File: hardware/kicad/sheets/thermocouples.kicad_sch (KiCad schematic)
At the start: 18 parts, among them J3 TC1_K, J8 TC2_K, U3 MAX31856MUD+, U5 MAX31856MUD+

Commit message: hardware: hierarchical schematic, ERC at 0/0, rev B.3
Applies items 1-3 of SCHEMATIC-REVIEW-2026-10-22.md.

ERC: the 173 lib_symbol_mismatch warnings were over-escaped quotes in the
embedded power symbols' Description strings; refreshed from the library.
The 18 off-grid power symbols are snapped and their stub wires redrawn.
The VIN and VLED global labels that existed only to carry a PWR_FLAG are
gone; the flags now sit on the nets they drive (J2.1, the VLED junction).
ERC reads 0 errors / 0 warnings with the documented SDO exclusion.

Hierarchy: no global labels remain. Each net that crosses sheets has one
hierarchical label per sheet, matching sheet pins on the root, and the
root wires those pins as a block diagram. Every other former global label
is a local label. The eight signal test points (TP4-TP11) move from the
test sheet to the mcu and ct sheets beside their nets, so the test block
needs no pins. KiCad names the nets /mcu/SPI_MISO etc.; netlist.py strips
the path, so the board's net names and the routing tables are unchanged
(182 components, 538 pads, 0 mismatches). single_global_label is now a
warning. check_sync_idempotent's collision fixture used the bare
"SPI_MISO" name and is updated, with a loud failure if its victims vanish.

Drawing: rev B.3 dated 2026-10-22 on every sheet, ct on A3 like the rest,
the three overflowing titles shortened, and the notes no longer refer to
design.py or to crystal load caps that no longer exist.

Co-Authored-By: Claude Fable 5.1 <noreply@anthropic.com>
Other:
- title: Bisque Kiln Controller - Thermocouple front-ends (MAX31856 x2) -> Bisque Kiln Controller - Thermocouple front-ends

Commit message: hardware: flags at their sources, tri-state MAX31856, Q4 flipped, make erc
Second batch from SCHEMATIC-REVIEW-2026-10-22.md (findings 5, 7, 14, 15,
16 and the local half of 19).

PWR_FLAGs: the power sheet's parked corner is gone. Each flag now sits
where its rail is created - J2.1 (VIN), J2.2 (GND), Q8 source (VIN_P),
L1 output (BUCK_5V) and J1 pin A4 (VBUS, on the mcu sheet) - with the
value text shown on all of them.

MAX31856: U3 and U5 now use bisque:MAX31856 from the new project library
bisque.kicad_sym (registered in sym-lib-table), a copy of the KiCad
symbol with SDO typed tri-state, which is what the part does while CS is
high. The ERC exclusion that papered over the shared SPI_MISO is removed;
ERC is clean with no exclusions.

Q4 is mirrored so the high-side P-FET reads source-up to +5V and drain
down to SSR_EN. One Value string per LCSC part (C38/C44/C45 22uF/25V,
R11 100R 1%); C46 moved 5 mm right to clear the longer text. Every test
point's Value is its net name (TP1 "+3V3" ... TP12 "WDT_CT_P"), so the
board's Value fields, the JLC BOM and the schematic PDF regenerate.

make erc runs kicad-cli ERC at every severity and fails on any
violation; lib_symbol_mismatch, endpoint_off_grid and
same_local_global_label are promoted to errors in the project. It is not
part of pcb-check or CI on purpose.

Board: sync changed only Value fields (0 re-netted); gerbers differ by
timestamp only; DRC 0; full make pcb-check passes.

Co-Authored-By: Claude Fable 5.1 <noreply@anthropic.com>
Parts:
- U3, U5: symbol Sensor_Temperature:MAX31856 -> bisque:MAX31856
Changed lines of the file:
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@@
 	)
 	(symbol
-		(lib_id "Sensor_Temperature:MAX31856")
+		(lib_id "bisque:MAX31856")
 		(at 186.69 80.01 0)
 		(unit 1)
@@
 	)
 	(symbol
-		(lib_id "Sensor_Temperature:MAX31856")
+		(lib_id "bisque:MAX31856")
 		(at 60.96 80.01 0)
 		(unit 1)

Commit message: hardware: honest symbols, real MPNs, U6 spares grounded, LCD_RST verified
Third batch from SCHEMATIC-REVIEW-2026-10-22.md (findings 6, 8, 11, 17,
18 and E1/E2).

Symbols: D8 is bisque:SMAJ30A (drawn as a zener with its cathode on the
rail, since the fitted TVS is unidirectional), Q5-Q7 are bisque:CJ2310
and U2 is bisque:TLV1117LV33, each a flattened copy of the stock symbol
with the fitted part's name, description and LCSC-hosted datasheet, so
no pin or wire moved. The stock D_TVS, 2N7002 and TLV1117-33 embeds are
gone from the sheets.

Sourcing: every one of the 160 assembled symbols now carries MPN (the
manufacturer's part number, from LCSC's product record for its C-number),
Manufacturer and Datasheet (LCSC's hosted PDF) beside LCSC. check_mpn.py
keeps LCSC tied to gen_jlc.LCSC and requires the other two to be present
and MPN not to be a bare C-number.

Drawing: J11's IN1_RAW/IN2_RAW labels read along their own wires instead
of across the connector; U6's unused Darlington inputs I4-I7 are tied to
GND (the board's F.Cu pour already covers them - 4 pads re-netted, 0
unconnected, DRC 0); the root notes record the retired designators and
the LCD_RST finding (the MSP4021's own schematic shows no pull-up on
RESET, so GPIO46 does not block download mode); the mcu sheet notes that
GPIO35/36 rule out R8 (octal PSRAM) modules.

The datasheet manifest maps the shared 22uF/25V sheet to the unified
value and exempts the test points' net-name values. Full make pcb-check
passes; gerbers differ by timestamp and the re-filled GND pour; 3D
renders refreshed.

Co-Authored-By: Claude Fable 5.1 <noreply@anthropic.com>
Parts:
- C13, C14, C15, C18, C19, C20: MPN C49678 -> CC0805KRX7R9BB104; Manufacturer (none) -> YAGEO
- C16, C17, C21, C22: MPN C1710 -> CL21B103KBANNNC; Manufacturer (none) -> Samsung Electro-Mechanics
- J3, J8: MPN C8465 -> WJ500V-5.08-2P; Manufacturer (none) -> KANGNEX
- R14, R15, R16, R17: MPN C17408 -> 0805W8F1000T5E; Manufacturer (none) -> UNI-ROYAL
- U3, U5: MPN C2653162 -> MAX31856MUD+T; Manufacturer (none) -> MAXIM

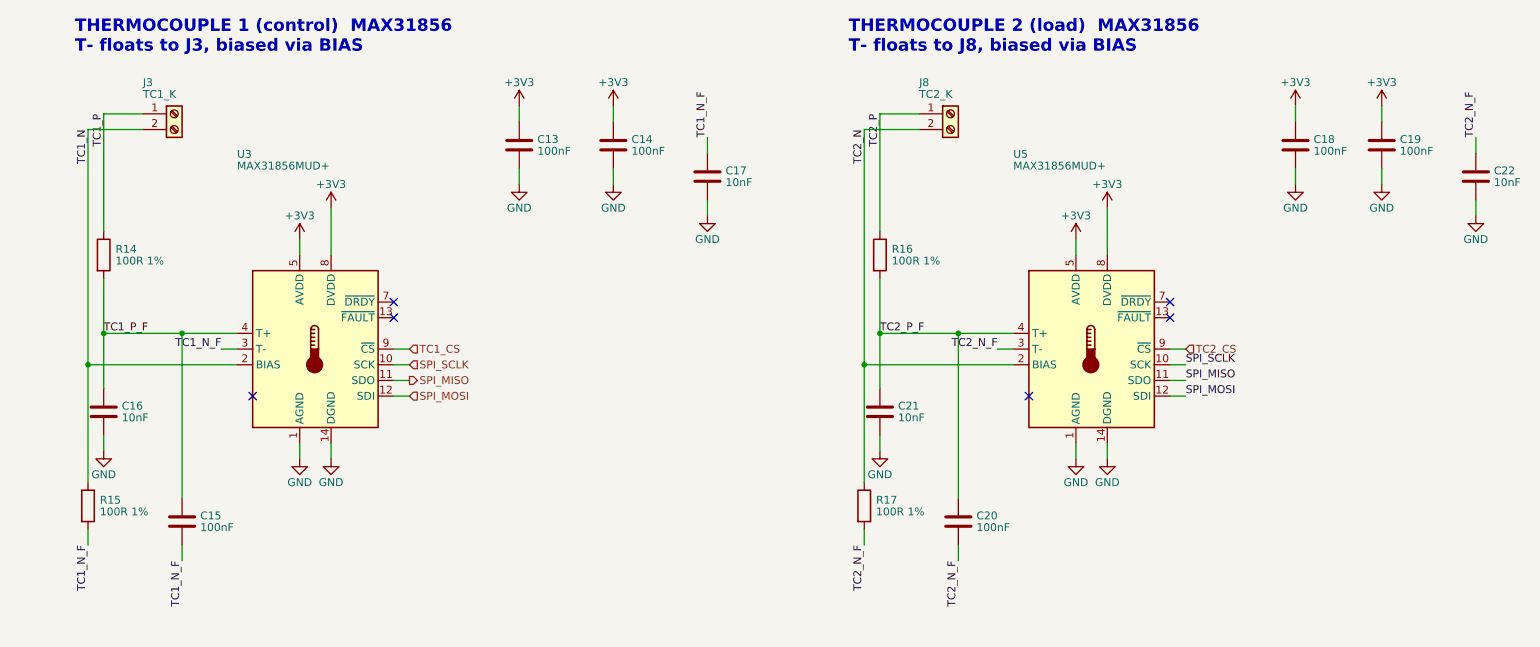
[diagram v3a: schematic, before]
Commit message: hardware: inline front-ends and decoupling at the pins (review 12, 13)
Fourth batch from SCHEMATIC-REVIEW-2026-10-22.md.

Thermocouples: each MAX31856 front-end is an inline chain - the terminal
mirrored so its pins face the IC, K+ and K- on two lines through their
100R, the 100 nF differential cap bridging the lines, the 10 nF caps to
GND off each line, BIAS returned to the raw K- node along the bottom -
and AVDD/DVDD rise to a short +3V3 rail with both 100 nF hanging from
it. The ICs slid 7.62 mm right to make room; nothing else moved.

CT: J12 feeds four lines at 17.78 mm pitch with the 5R1 burden between
each pair, the 1k series parts in the path, the 33 nF to GND off each
filtered node and the 1k references off the N lines; the filtered nodes
end in the CTA_F / CTA_FN / CTB_F labels the ADE7953 pins already
carried. D6 keeps a label-fed clamp block beside the chain. VDD, VINTD
and VINTA each get a rail at the IC's top pin with their two caps on it;
R37/R38 moved 7.62 mm right to clear them.

io: IN1-IN3 are three identical rows - J11 mirrored, 1k in the path, the
10k pull-up above and 100 nF below the node, the hierarchical label at
the end - with D5's clamp block below them.

mcu: C6/C7 hang from U1's 3V3 pin. power: U2 is drawn as an inline
5 V -> 3.3 V chain with C1/C2 on its input and C3/C4 on its output in
the row the caps already occupied; LED2/R9 slid right.

Every pin landed on wiring by construction (the geometry helper checks
each symbol's pins against the wires), ERC is clean, the layout checker
reports no overlaps, the netlist still has 108 nets and the board sync
re-netted nothing. Fab outputs regenerated (schematic PDF, timestamps).

Co-Authored-By: Claude Fable 5.1 <noreply@anthropic.com>
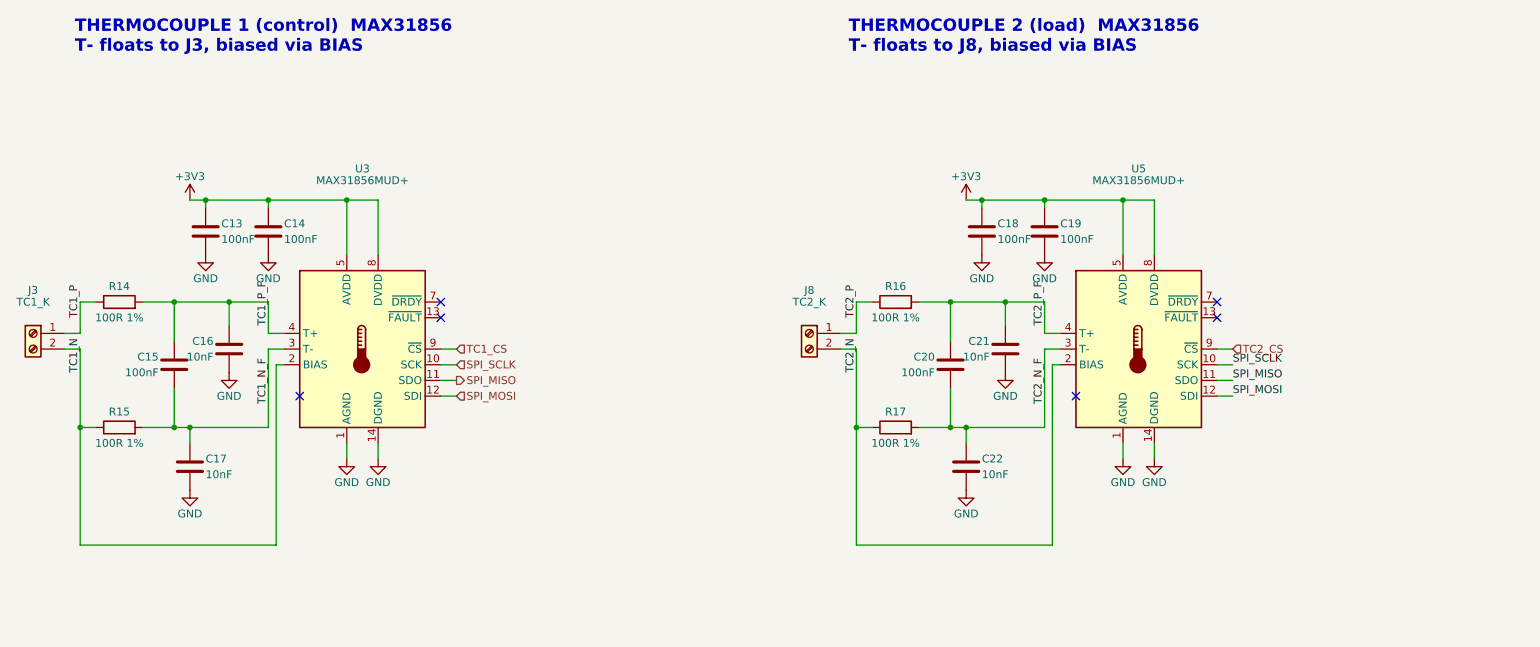
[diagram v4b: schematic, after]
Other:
- moved on the sheet: C13, C14, C15, C16, C17, C18, C19, C20, C21, C22, J3, J8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

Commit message: hardware: BOM from the schematic, JLCPCB fits every part
BOM.csv is now kicad-cli's export of the schematic itself (make pcb-fab),
so every symbol not marked "Exclude from BOM" is on it; gen_jlc reads the
same flags instead of a hand-kept NOT_ASSEMBLED/HAND_SOLDER table.

JLCPCB assembly of the 12 through-hole parts plus LED1 costs ~$22 an order
against ~$110 for partial assembly and a Mouser order, so they are no
longer hand-fitted. Their Assembly field reads "Optional hand solder - JLC
assembles; untick at JLC to fit by hand"; setting it back to "HAND SOLDER"
makes a part hand-fitted again. JLC_PLACEMENT gains fitted corrections for
the six new LCSC parts (J7 needs 180 deg).

LED1 moves to the in-stock WS2812B-V5/W (C2874885): same pinout, and its
VIH of 0.63*VDD (~2.6 V at VLED) is below the old part's 2.7 V.
mouser-order.csv now holds only the mating housings and crimps.

Co-Authored-By: Claude Opus 5.5 <noreply@anthropic.com>
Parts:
- J3, J8: Assembly (none) -> Optional hand solder - JLC assembles; untick at JLC to fit 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
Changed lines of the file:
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@@
 			)
 		)
-	)
+		(property "Assembly" "Optional hand solder - JLC assembles; untick at JLC to fit by hand"
+			(at 15.24 77.47 0)
+			(hide yes)
+			(effects
+				(font
+					(size 1.27 1.27)
+				)
+			)
+		))
 	(symbol
 		(lib_id "Device:R")
@@
 			)
 		)
-	)
+		(property "Assembly" "Optional hand solder - JLC assembles; untick at JLC to fit by hand"
+			(at 140.97 77.47 0)
+			(hide yes)
+			(effects
+				(font
+					(size 1.27 1.27)
+				)
+			)
+		))
 	(symbol
 		(lib_id "power:GND")
